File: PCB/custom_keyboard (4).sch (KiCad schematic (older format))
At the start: 412 parts, among them IC1 FE2.1, J1 USB_A, J2 USB_A, J3 USB_A, J4 Conn_01x03_Male, J5 AVR-ISP-6, Q1 DTC123J, SW1 SW_Push, U1 24LC02, U10 PRTR5V0U2X, U11 XC6206P332MR, U12 74LVC1G34, U2 PRTR5V0U2X, U3 PRTR5V0U2X, U4 PRTR5V0U2X, U5 PRTR5V0U2X, U6 PRTR5V0U2X, U7 PRTR5V0U2X, U8 PRTR5V0U2X, U9 STM32F303CBTx, Y1 12MHz, Y2 8MHz, Y3 32.768kHZ

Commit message: Updated footprints
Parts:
- added R47: 500, Resistor_SMD:R_0805_2012Metric, symbol Device:R_Small
- MX1, MX10, MX11, MX12, MX13, MX14, MX15, MX16, MX17, MX18, MX19, MX2, MX20, MX21, MX22, MX23, MX24, MX25, MX26, MX27, MX28, MX3, MX30, MX31, MX32, MX33, MX35, MX36, MX37, MX38, MX39, MX4, MX40, MX41, MX42, MX43, MX44, MX45, MX46, MX48, MX49, MX5, MX50, MX51, MX53, MX54, MX55, MX56, MX57, MX58, MX59, MX6, MX60, MX61, MX62, MX63, MX65, MX67, MX68, MX69, MX7, MX70, MX71, MX72, MX73, MX74, MX75, MX76, MX78, MX79, MX8, MX88, MX89, MX9, MX90: footprint CherryMX_PCB_KailhSocket_LTST-A683CEGBW:CherryMX_1.00u_PCB_KailhSocket_LTST-A683CEGBW -> custom-footprints:CherryMX_1.00u_PCB_KailhSocket_LTST-A683CEGBW
- MX29: footprint CherryMX_PCB_KailhSocket_LTST-A683CEGBW:CherryMX_1.00u_PCB_KailhSocket_LTST-A683CEGBW -> custom-footprints:CherryMX_2.00u_PCB_KailhSocket_LTST-A683CEGBW
- MX34, MX47: footprint CherryMX_PCB_KailhSocket_LTST-A683CEGBW:CherryMX_1.00u_PCB_KailhSocket_LTST-A683CEGBW -> custom-footprints:CherryMX_1.50u_PCB_KailhSocket_LTST-A683CEGBW
- MX52: footprint CherryMX_PCB_KailhSocket_LTST-A683CEGBW:CherryMX_1.00u_PCB_KailhSocket_LTST-A683CEGBW -> custom-footprints:CherryMX_1.75u_PCB_KailhSocket_LTST-A683CEGBW
- MX64, MX66: footprint CherryMX_PCB_KailhSocket_LTST-A683CEGBW:CherryMX_1.00u_PCB_KailhSocket_LTST-A683CEGBW -> custom-footprints:CherryMX_2.25u_PCB_KailhSocket_LTST-A683CEGBW
- MX77: footprint CherryMX_PCB_KailhSocket_LTST-A683CEGBW:CherryMX_1.00u_PCB_KailhSocket_LTST-A683CEGBW -> custom-footprints:CherryMX_2.75u_PCB_KailhSocket_LTST-A683CEGBW
- MX80, MX81, MX82, MX84, MX85, MX86, MX87: footprint CherryMX_PCB_KailhSocket_LTST-A683CEGBW:CherryMX_1.00u_PCB_KailhSocket_LTST-A683CEGBW -> custom-footprints:CherryMX_1.25u_PCB_KailhSocket_LTST-A683CEGBW
- MX83: footprint CherryMX_PCB_KailhSocket_LTST-A683CEGBW:CherryMX_1.00u_PCB_KailhSocket_LTST-A683CEGBW -> custom-footprints:CherryMX_6.25u_PCB_KailhSocket_LTST-A683CEGBW
- renumbered C21 to C1, C37 to C10, C1 to C11, C2 to C12, C3 to C13, C4 to C14, C30 to C15, C31 to C16, C32 to C17, C33 to C18, C34 to C19, C29 to C2, C35 to C20, C36 to C21, C38 to C22, C39 to C23, C5 to C24, C6 to C25, C7 to C26, C8 to C27, C9 to C28, C10 to C29, C22 to C3, C11 to C30, C12 to C31, C13 to C32, C14 to C33, C15 to C34, C16 to C35, C17 to C36, C18 to C37, C19 to C38, C20 to C39, C23 to C4, C24 to C5, C25 to C6, C26 to C7, C27 to C8, C28 to C9, D3 to D1, D1 to D2, D2 to D3, F5 to F2, F6 to F3, F2 to F4, F7 to F5, F3 to F6, F4 to F7, FB5 to FB2, FB6 to FB3, FB2 to FB4, FB7 to FB5, FB3 to FB6, FB4 to FB7, J4 to J2, J2 to J3, J3 to J4, C50 to LC10, C51 to LC11, C52 to LC12, C53 to LC13, C54 to LC14, LC2 to LC15, LC3 to LC16, LC4 to LC17, C55 to LC18, C56 to LC19, C42 to LC2, C57 to LC20, C58 to LC21, C59 to LC22, C60 to LC23, C61 to LC24, C62 to LC25, C63 to LC26, C64 to LC27, C65 to LC28, C66 to LC29, C43 to LC3, C67 to LC30, C68 to LC31, C69 to LC32, LC5 to LC33, LC6 to LC34, LC7 to LC35, C70 to LC36, C71 to LC37, C72 to LC38, C73 to LC39, C44 to LC4, C74 to LC40, C75 to LC41, C76 to LC42, C77 to LC43, C78 to LC44, C79 to LC45, C80 to LC46, C81 to LC47, C82 to LC48, C83 to LC49, C45 to LC5, C84 to LC50, LC8 to LC51, LC9 to LC52, LC10 to LC53, C85 to LC54, C86 to LC55, C87 to LC56, C88 to LC57, C89 to LC58, C90 to LC59, C46 to LC6, C91 to LC60, C92 to LC61, C93 to LC62, C94 to LC63, C95 to LC64, LC11 to LC65, LC12 to LC66, LC13 to LC67, C96 to LC68, C97 to LC69, C47 to LC7, C98 to LC70, C99 to LC71, C100 to LC72, C101 to LC73, C102 to LC74, C103 to LC75, C104 to LC76, C105 to LC77, C106 to LC78, LC14 to LC79, C48 to LC8, LC15 to LC80, LC16 to LC81, C107 to LC82, C108 to LC83, C109 to LC84, C110 to LC85, C111 to LC86, C112 to LC87, C113 to LC88, C114 to LC89, C49 to LC9, C115 to LC90, R16 to R1, R25 to R10, R26 to R11, R17 to R12, R18 to R13, R19 to R14, R20 to R15, R21 to R16, R27 to R17, R28 to R18, R29 to R19, R1 to R2, R30 to R20, R5 to R21, R6 to R22, R7 to R23, R8 to R24, R9 to R25, R31 to R26, R33 to R27, R34 to R28, R35 to R29, R23 to R3, R32 to R30, R39 to R31, R36 to R32, R40 to R33, R10 to R34, R42 to R35, R43 to R36, R11 to R37, R41 to R38, R37 to R39, R2 to R4, R38 to R40, R12 to R41, R44 to R42, R45 to R43, R46 to R44, R13 to R45, R14 to R46, R15 to R5, R24 to R6, R22 to R7, R3 to R8, R4 to R9, U5 to U10, U6 to U3, U7 to U4, U3 to U5, U10 to U6, U4 to U7, Y2 to Y1, Y3 to Y2, Y1 to Y3
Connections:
- net ROT1_COL is gone; now on net COL0: ROT1.S1
- net ROT2_COL is gone; now on net COL17: ROT2.S1
- net +5V: now also LC1.2, LC10.2, LC11.2, LC12.2, LC13.2, LC14.2, LC15.2, LC16.2, LC17.2, LC18.2, LC19.2, LC2.2, LC20.2, LC21.2, LC22.2, LC23.2, LC24.2, LC25.2, LC26.2, LC27.2, LC28.2, LC29.2, LC3.2, LC30.2, LC31.2, LC32.2, LC33.2, LC34.2, LC35.2, LC36.2, LC37.2, LC38.2, LC39.2, LC4.2, LC40.2, LC41.2, LC42.2, LC43.2, LC44.2, LC45.2, LC46.2, LC47.2, LC48.2, LC49.2, LC5.2, LC50.2, LC51.2, LC52.2, LC53.2, LC54.2, LC55.2, LC56.2, LC57.2, LC58.2, LC59.2, LC6.2, LC60.2, LC61.2, LC62.2, LC63.2, LC64.2, LC65.2, LC66.2, LC67.2, LC68.2, LC69.2, LC7.2, LC70.2, LC71.2, LC72.2, LC73.2, LC74.2, LC75.2, LC76.2, LC77.2, LC78.2, LC79.2, LC8.2, LC80.2, LC81.2, LC82.2, LC83.2, LC84.2, LC85.2, LC86.2, LC87.2, LC88.2, LC89.2, LC9.2, LC90.2, MX1.6 (VDD), MX10.6 (VDD), MX11.6 (VDD), MX12.6 (VDD), MX13.6 (VDD), MX14.6 (VDD), MX15.6 (VDD), MX16.6 (VDD), MX17.6 (VDD), MX18.6 (VDD), MX19.6 (VDD), MX2.6 (VDD), MX20.6 (VDD), MX21.6 (VDD), MX22.6 (VDD), MX23.6 (VDD), MX24.6 (VDD), MX25.6 (VDD), MX26.6 (VDD), MX27.6 (VDD), MX28.6 (VDD), MX29.6 (VDD), MX3.6 (VDD), MX30.6 (VDD), MX31.6 (VDD), MX32.6 (VDD), MX33.6 (VDD), MX34.6 (VDD), MX35.6 (VDD), MX36.6 (VDD), MX37.6 (VDD), MX38.6 (VDD), MX39.6 (VDD), MX4.6 (VDD), MX40.6 (VDD), MX41.6 (VDD), MX42.6 (VDD), MX43.6 (VDD), MX44.6 (VDD), MX45.6 (VDD), MX46.6 (VDD), MX47.6 (VDD), MX48.6 (VDD), MX49.6 (VDD), MX5.6 (VDD), MX50.6 (VDD), MX51.6 (VDD), MX52.6 (VDD), MX53.6 (VDD), MX54.6 (VDD), MX55.6 (VDD), MX56.6 (VDD), MX57.6 (VDD), MX58.6 (VDD), MX59.6 (VDD), MX6.6 (VDD), MX60.6 (VDD), MX61.6 (VDD), MX62.6 (VDD), MX63.6 (VDD), MX64.6 (VDD), MX65.6 (VDD), MX66.6 (VDD), MX67.6 (VDD), MX68.6 (VDD), MX69.6 (VDD), MX7.6 (VDD), MX70.6 (VDD), MX71.6 (VDD), MX72.6 (VDD), MX73.6 (VDD), MX74.6 (VDD), MX75.6 (VDD), MX76.6 (VDD), MX77.6 (VDD), MX78.6 (VDD), MX79.6 (VDD), MX8.6 (VDD), MX80.6 (VDD), MX81.6 (VDD), MX82.6 (VDD), MX83.6 (VDD), MX84.6 (VDD), MX85.6 (VDD), MX86.6 (VDD), MX87.6 (VDD), MX88.6 (VDD), MX89.6 (VDD), MX9.6 (VDD), MX90.6 (VDD)
- net BKL_DATA_IN: now also R47.1
- net at MX1.4 (DIN): now also R47.2

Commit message: Routed everything regarding the USB hub
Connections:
- net COL17: no longer ROT2.S1
- net HUB_PORT2_D+: now also R33.2; no longer R24.2
- net HUB_PORT2_D-: now also R31.2; no longer R25.2
- net HUB_PORT5_D+: now also R6.1; no longer R3.2
- net HUB_PORT5_D-: now also R3.1; no longer R6.2
- net HUB_PORT6_D+: now also R24.2; no longer R19.2
- net HUB_PORT6_D-: now also R25.2; no longer R20.2
- net HUB_PORT7_D+: now also R19.2; no longer R31.2
- net HUB_PORT7_D-: now also R20.2; no longer R33.2
- net D-: now reaches U3.3 (IO2), USB2.5 (DN2), USB2.7 (DN1)
- net D-: now also J1.2 (D-), J3.2 (D-), J4.2 (D-), R2.1, R20.1, R25.1, R3.2, R31.1, R37.1, R43.1, R46.1, U10.3 (IO2), U2.3 (IO2), U4.3 (IO2), U5.3 (IO2), U6.3 (IO2), U7.3 (IO2), U9.32 (PA11), USB1.5 (DN2), USB1.7 (DN1), USB3.5 (DN2), USB3.7 (DN1), USB4.5 (DN2), USB4.7 (DN1); no longer R3.1
- net D+: now reaches U3.2 (IO1), USB2.6 (DP1), USB2.8 (DP2)
- net D+: now also J1.3 (D+), J3.3 (D+), J4.3 (D+), R19.1, R24.1, R33.1, R34.1, R4.1, R44.1, R45.1, R6.2, U10.2 (IO1), U2.2 (IO1), U4.2 (IO1), U5.2 (IO1), U6.2 (IO1), U7.2 (IO1), U9.33 (PA12), USB1.6 (DP1), USB1.8 (DP2), USB3.6 (DP1), USB3.8 (DP2), USB4.6 (DP1), USB4.8 (DP2); no longer R6.1
- new net ROT2_COL: ROT2.S1
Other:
- moved on the sheet: C11, C12, C14, C24, C26, C27, C28, C29, C30, C31, C32, C33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

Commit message: Placed microcontroller components in position
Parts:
- removed R39, R40: 22, Resistor_SMD:R_0805_2012Metric, symbol Device:R_Small
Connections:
- net BKL_DATA_IN_3V3: now also U9.25 (PB12); no longer U9.38 (PA15)
- net COL10: now also U9.18 (PB0); no longer U9.43 (PB7)
- net COL11: now also U9.39 (PB3); no longer U9.45 (PB8)
- net COL12: now also U9.20 (PB2); no longer U9.46 (PB9)
- net COL15: now also U9.38 (PA15); no longer U9.25 (PB12)
- net COL9: now also U9.19 (PB1); no longer U9.42 (PB6)
- net KEYBOARD_D+: now also U8.2 (IO1)
- net KEYBOARD_D-: now also U8.3 (IO2)
- net ROT1_ROW: now also U9.46 (PB9); no longer U9.18 (PB0)
- net ROW1: now also U9.45 (PB8); no longer U9.19 (PB1)
- net ROW2: now also U9.43 (PB7); no longer U9.20 (PB2)
- net ROW3: now also U9.42 (PB6); no longer U9.39 (PB3)
- net ROW4: now also U9.41 (PB5); no longer U9.40 (PB4)
- net ROW5: now also U9.40 (PB4); no longer U9.41 (PB5)
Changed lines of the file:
@@
 Wire Wire Line
 	6250 17900 6350 17900
-Text GLabel 9600 16350 2    50   Input ~ 0
+Text GLabel 9400 16350 2    50   Input ~ 0
 KEYBOARD_D+
-Text GLabel 8000 16350 0    50   Input ~ 0
+Text GLabel 8200 16350 0    50   Input ~ 0
 KEYBOARD_D-
 $Comp
@@
 Text GLabel 5150 17600 2    50   Input ~ 0
 KEYBOARD_SCL
-$Comp
-L Device:R_Small R40
-U 1 1 A720CCE9
-P 9400 16350
-F 0 "R40" V 9204 16350 50  0000 C CNN
-F 1 "22" V 9295 16350 50  0000 C CNN
-F 2 "Resistor_SMD:R_0805_2012Metric" H 9400 16350 50  0001 C CNN
-F 3 "~" H 9400 16350 50  0001 C CNN
-	1    9400 16350
-	0    1    1    0
-$EndComp
-$Comp
-L Device:R_Small R39
-U 1 1 A7E3297A
-P 8200 16350
-F 0 "R39" V 8004 16350 50  0000 C CNN
-F 1 "22" V 8095 16350 50  0000 C CNN
-F 2 "Resistor_SMD:R_0805_2012Metric" H 8200 16350 50  0001 C CNN
-F 3 "~" H 8200 16350 50  0001 C CNN
-	1    8200 16350
-	0    1    1    0
-$EndComp
-Wire Wire Line
-	8000 16350 8100 16350
-Wire Wire Line
-	9100 16350 9300 16350
-Wire Wire Line
-	9500 16350 9600 16350
 Wire Notes Line
 	10250 15700 10250 16850
@@
 	7350 15700 10250 15700
 Wire Wire Line
-	8300 16350 8500 16350
-Wire Wire Line
 	6150 17900 6250 17900
 Wire Wire Line
@@
 Text GLabel 5150 16700 2    50   Input ~ 0
 COL0
-Text GLabel 3450 17300 0    50   Input ~ 0
+Text GLabel 3450 16800 0    50   Input ~ 0
 COL9
 Text GLabel 5150 17500 2    50   Input ~ 0
@@
 Text GLabel 5150 17100 2    50   Input ~ 0
 COL4
-Text GLabel 3450 17400 0    50   Input ~ 0
+Text GLabel 3450 16700 0    50   Input ~ 0
 COL10
-Text GLabel 3450 17500 0    50   Input ~ 0
+Text GLabel 3450 17000 0    50   Input ~ 0
 COL11
 Text GLabel 5500 18000 2    50   Input ~ 0
@@
 Text GLabel 5500 18100 2    50   Input ~ 0
 COL16
-Text GLabel 3450 17900 0    50   Input ~ 0
+Text GLabel 5500 18200 2    50   Input ~ 0
 COL15
 Text GLabel 3450 17800 0    50   Input ~ 0
@@
 Text GLabel 3450 17700 0    50   Input ~ 0
 COL13
-Text GLabel 3450 17600 0    50   Input ~ 0
+Text GLabel 3450 16900 0    50   Input ~ 0
 COL12
-Text GLabel 3450 17100 0    50   Input ~ 0
-ROW4
 Text GLabel 3450 17200 0    50   Input ~ 0
+ROW4
+Text GLabel 3450 17100 0    50   Input ~ 0
 ROW5
-Text GLabel 3450 17000 0    50   Input ~ 0
+Text GLabel 3450 17300 0    50   Input ~ 0
 ROW3
-Text GLabel 3450 16900 0    50   Input ~ 0
+Text GLabel 3450 17400 0    50   Input ~ 0
 ROW2
-Text GLabel 3450 16800 0    50   Input ~ 0
+Text GLabel 3450 17500 0    50   Input ~ 0
 ROW1
-Text GLabel 3450 16700 0    50   Input ~ 0
+Text GLabel 3450 17600 0    50   Input ~ 0
 ROW0
-Text GLabel 5500 18200 2    50   Input ~ 0
+Text GLabel 3450 17900 0    50   Input ~ 0
 BKL_DATA_IN_3V3
 Text GLabel 3450 18000 0    50   Input ~ 0
@@
 	1    0    0    -1
 $EndComp
+Wire Wire Line
+	8200 16350 8500 16350
+Wire Wire Line
+	9100 16350 9400 16350
 $EndSCHEMATC

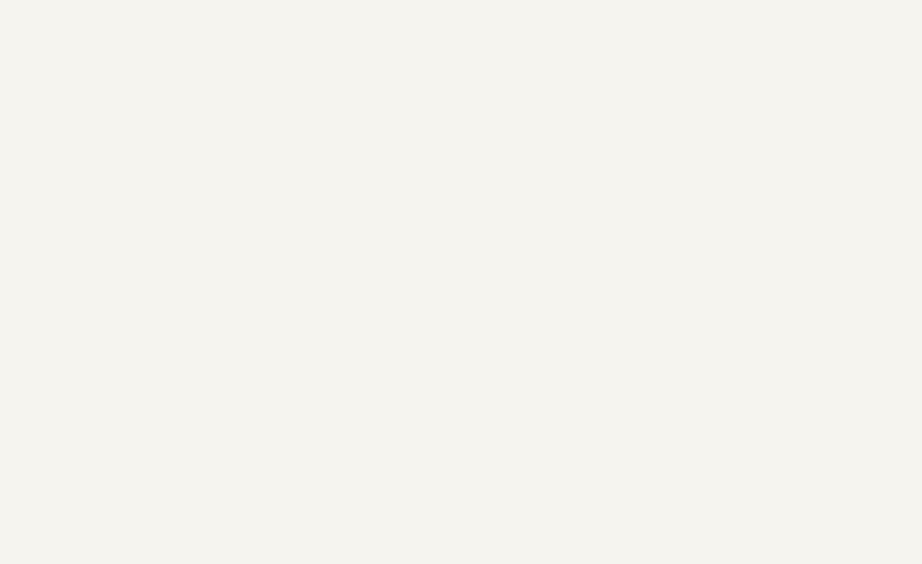
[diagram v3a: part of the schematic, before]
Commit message: Added mounting holes
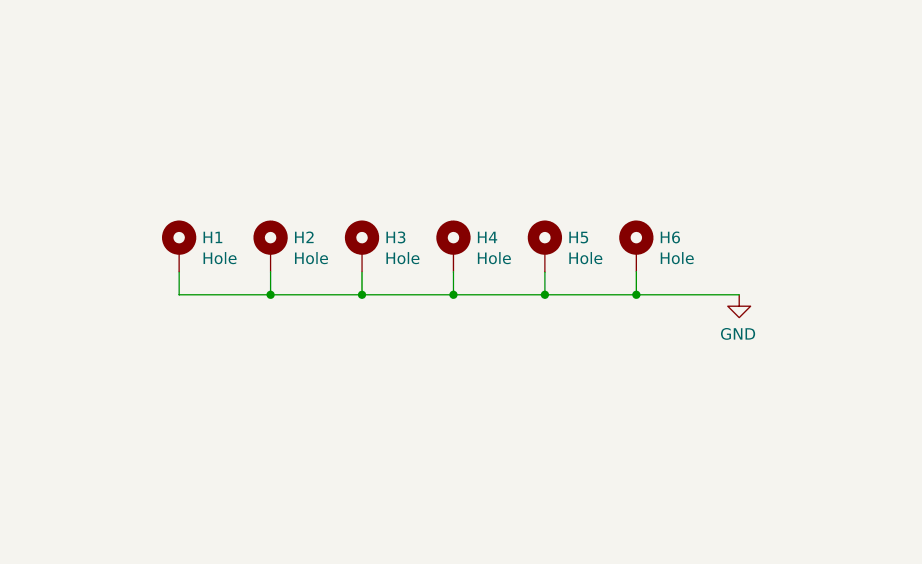
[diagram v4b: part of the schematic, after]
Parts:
- added H1, H2, H3, H4, H5, H6: Hole, MountingHole:MountingHole_3.2mm_M3_Pad, symbol Mechanical:MountingHole_Pad
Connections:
- net GND: now also H1.1, H2.1, H3.1, H4.1, H5.1, H6.1
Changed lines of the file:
@@
 Wire Wire Line
 	9100 16350 9400 16350
+$Comp
+L Mechanical:MountingHole_Pad H4
+U 1 1 6FB1B5C9
+P 12800 20000
+F 0 "H4" H 12900 20049 50  0000 L CNN
+F 1 "Hole" H 12900 19958 50  0000 L CNN
+F 2 "MountingHole:MountingHole_3.2mm_M3_Pad" H 12800 20000 50  0001 C CNN
+F 3 "~" H 12800 20000 50  0001 C CNN
+	1    12800 20000
+	1    0    0    -1
+$EndComp
+$Comp
+L Mechanical:MountingHole_Pad H5
+U 1 1 6FB1C97B
+P 13200 20000
+F 0 "H5" H 13300 20049 50  0000 L CNN
+F 1 "Hole" H 13300 19958 50  0000 L CNN
+F 2 "MountingHole:MountingHole_3.2mm_M3_Pad" H 13200 20000 50  0001 C CNN
+F 3 "~" H 13200 20000 50  0001 C CNN
+	1    13200 20000
+	1    0    0    -1
+$EndComp
+$Comp
+L Mechanical:MountingHole_Pad H6
+U 1 1 6FB1CEC9
+P 13600 20000
+F 0 "H6" H 13700 20049 50  0000 L CNN
+F 1 "Hole" H 13700 19958 50  0000 L CNN
+F 2 "MountingHole:MountingHole_3.2mm_M3_Pad" H 13600 20000 50  0001 C CNN
+F 3 "~" H 13600 20000 50  0001 C CNN
+	1    13600 20000
+	1    0    0    -1
+$EndComp
+$Comp
+L power:GND #PWR0283
+U 1 1 7017E3FA
+P 14050 20200
+F 0 "#PWR0283" H 14050 19950 50  0001 C CNN
+F 1 "GND" H 14055 20027 50  0000 C CNN
+F 2 "" H 14050 20200 50  0001 C CNN
+F 3 "" H 14050 20200 50  0001 C CNN
+	1    14050 20200
+	-1   0    0    -1
+$EndComp
+Wire Wire Line
+	14050 20200 13600 20200
+Wire Wire Line
+	12800 20200 12800 20100
+Wire Wire Line
+	13200 20100 13200 20200
+Wire Wire Line
+	13600 20100 13600 20200
+$Comp
+L Mechanical:MountingHole_Pad H1
+U 1 1 72E52B19
+P 11600 20000
+F 0 "H1" H 11700 20049 50  0000 L CNN
+F 1 "Hole" H 11700 19958 50  0000 L CNN
+F 2 "MountingHole:MountingHole_3.2mm_M3_Pad" H 11600 20000 50  0001 C CNN
+F 3 "~" H 11600 20000 50  0001 C CNN
+	1    11600 20000
+	1    0    0    -1
+$EndComp
+$Comp
+L Mechanical:MountingHole_Pad H2
+U 1 1 72E561AB
+P 12000 20000
+F 0 "H2" H 12100 20049 50  0000 L CNN
+F 1 "Hole" H 12100 19958 50  0000 L CNN
+F 2 "MountingHole:MountingHole_3.2mm_M3_Pad" H 12000 20000 50  0001 C CNN
+F 3 "~" H 12000 20000 50  0001 C CNN
+	1    12000 20000
+	1    0    0    -1
+$EndComp
+$Comp
+L Mechanical:MountingHole_Pad H3
+U 1 1 72E561B5
+P 12400 20000
+F 0 "H3" H 12500 20049 50  0000 L CNN
+F 1 "Hole" H 12500 19958 50  0000 L CNN
+F 2 "MountingHole:MountingHole_3.2mm_M3_Pad" H 12400 20000 50  0001 C CNN
+F 3 "~" H 12400 20000 50  0001 C CNN
+	1    12400 20000
+	1    0    0    -1
+$EndComp
+Wire Wire Line
+	11600 20200 11600 20100
+Wire Wire Line
+	12000 20100 12000 20200
+Wire Wire Line
+	12400 20100 12400 20200
+Wire Wire Line
+	11600 20200 12000 20200
+Connection ~ 13600 20200
+Connection ~ 12000 20200
+Wire Wire Line
+	12000 20200 12400 20200
+Connection ~ 12400 20200
+Wire Wire Line
+	12400 20200 12800 20200
+Connection ~ 12800 20200
+Wire Wire Line
+	12800 20200 13200 20200
+Connection ~ 13200 20200
+Wire Wire Line
+	13200 20200 13600 20200
 $EndSCHEMATC
